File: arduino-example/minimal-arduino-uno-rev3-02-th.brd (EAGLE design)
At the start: 67.3 x 33 mm, 15 parts, among them J1 3x2 M, J3 POWERSUPPLY_DC21MMX, U1 NCP1117ST50T3G, X1 CSTCE16M0V53-R0 16MHZ

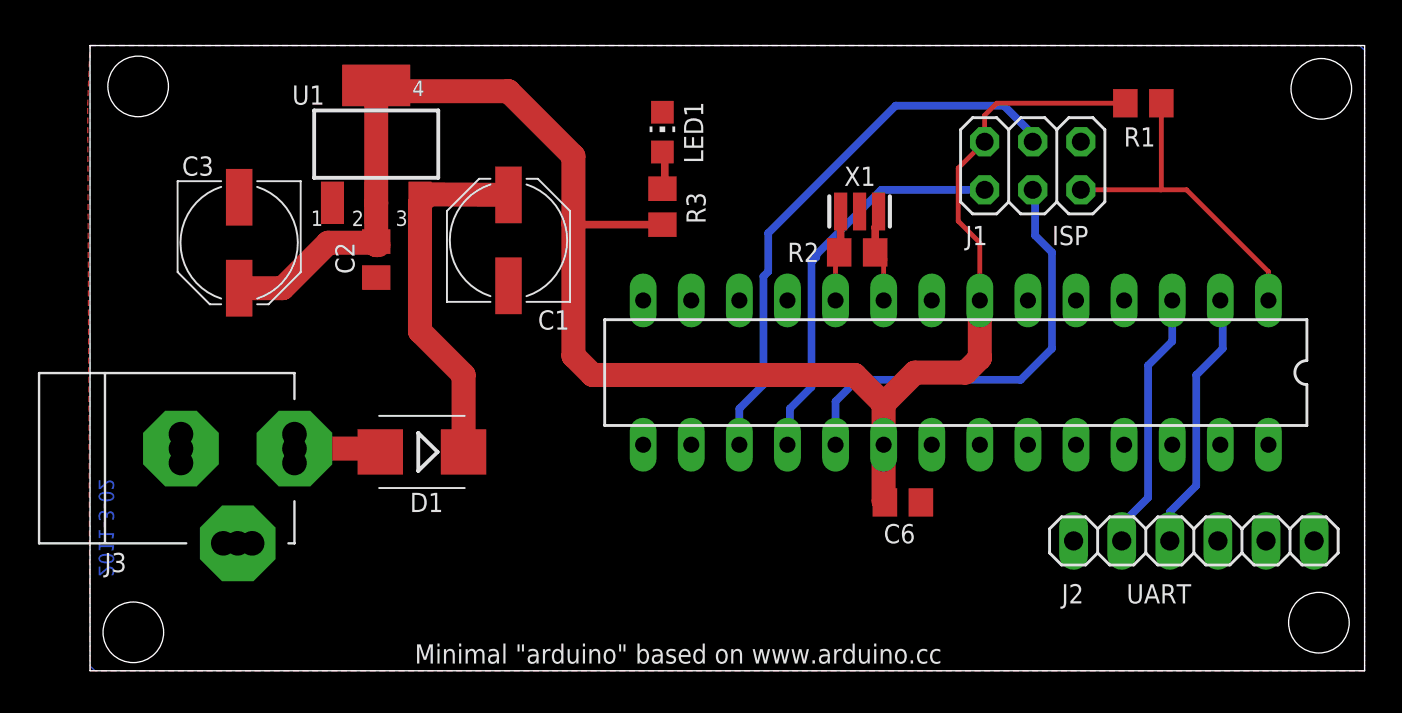
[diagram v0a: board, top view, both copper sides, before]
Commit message: Updated minimal arduino board.
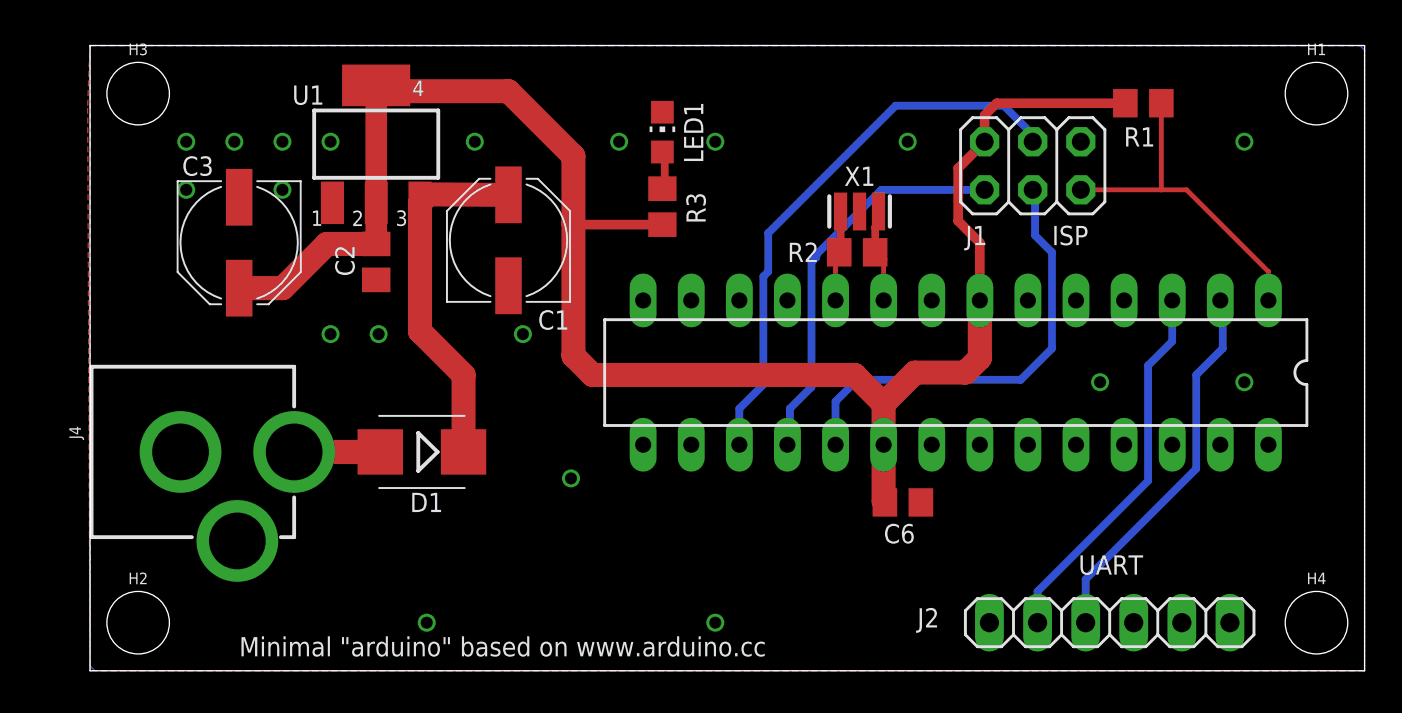
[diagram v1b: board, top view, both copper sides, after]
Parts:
- removed J3: POWERSUPPLY_DC21MMX, SmartPrj:POWERSUPPLY_DC-21MM
- added H1, H2, H3, H4: STAND-OFF, SparkFun-Hardware:STAND-OFF
- added J4: POWER_JACK, SparkFun-Connectors:POWER_JACK_PTH
- moved J2 6.20 mm to (53.8, 2.54)
- moved C2 0.13 mm to (15.1, 21.6)
- renumbered ZU4 to U4
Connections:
- net N$1 renamed RXD
- net N$2 renamed TXD
- net GND: now also J4.GND, J4.GNDBREAK; no longer J3.1, J3.3
- net PWRIN: now also J4.PWR; no longer J3.2
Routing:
- net RXD: track 14.2 -> 20.3 mm
- net TXD: track 14.4 -> 20.6 mm
- net +5V: track 95.0 -> 94.2 mm
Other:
- board text removed: "2011-3-02"
